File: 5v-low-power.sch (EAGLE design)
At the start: 34 parts, among them J1 Bypass, J2 En, J3 12v, J4 5V Out, J5 LED EN, J6 POWERPOLE_POWER10AWG, J7 POWERPOLE_POWER10AWG, Q1 SI4532ADY, U1 LT1934ES6TRMPBF

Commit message: changed to correct powerpole version added current rating onto docu layer
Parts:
- J6, J7: value POWERPOLE_POWER10AWG -> POWERPOLE_POWER25A; device powerpoles:POWERPOLE_POWER10AWG -> powerpoles:POWERPOLE_POWER25A
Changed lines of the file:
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@@
 <part name="GND" library="testpad" deviceset="TP" device="B1,27" value="5V B"/>
 <part name="J3" library="farnell-parts" deviceset="2-PIN-MOLEX" device="" value="12v"/>
-<part name="J6" library="powerpoles" deviceset="POWERPOLE_POWER" device="10AWG"/>
-<part name="J7" library="powerpoles" deviceset="POWERPOLE_POWER" device="10AWG"/>
+<part name="J6" library="powerpoles" deviceset="POWERPOLE_POWER" device="25A" value="POWERPOLE_POWER25A"/>
+<part name="J7" library="powerpoles" deviceset="POWERPOLE_POWER" device="25A" value="POWERPOLE_POWER25A"/>
 </parts>
 <sheets>

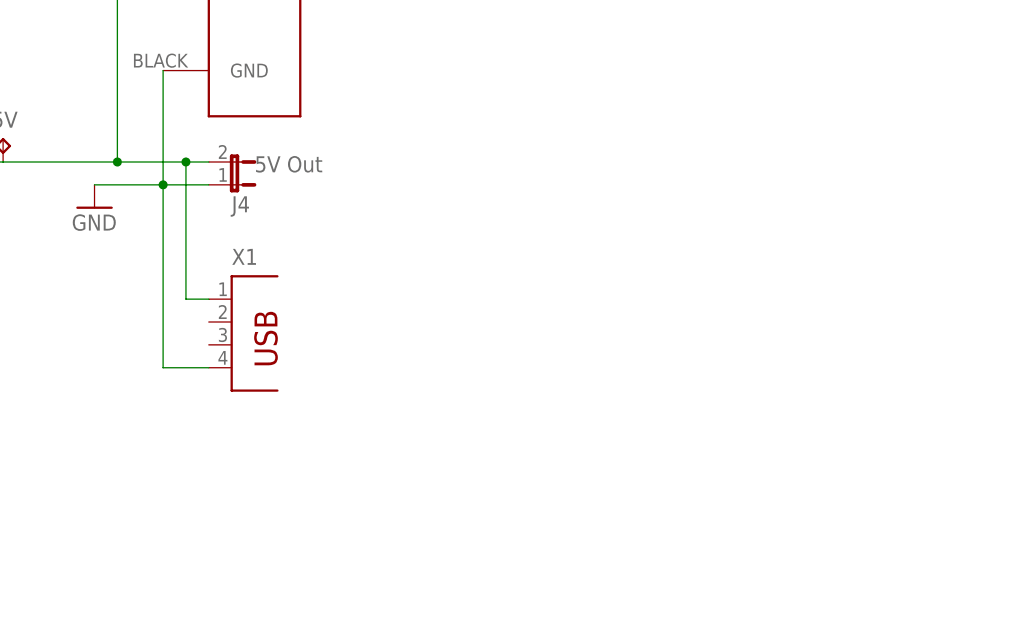
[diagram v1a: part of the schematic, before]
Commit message: Added additional USB footprints and rotated some powerpoles
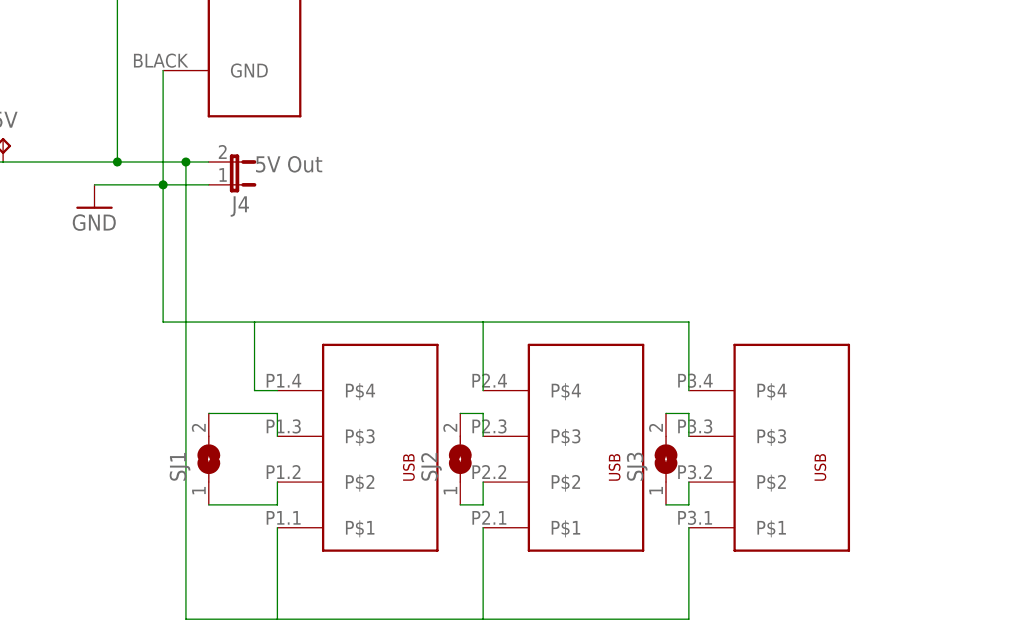
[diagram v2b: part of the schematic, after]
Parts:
- removed X1: (no value), con-berg:PN87520
- added SJ1, SJ2, SJ3: (no value), jumper:SJ
- added U$1: USB_DUAL_VERT+HORIZTRIPPLE, power:USB_DUAL_VERT+HORIZTRIPPLE
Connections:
- new net N$2: SJ1.2, U$1G$1.P$3
- new net N$4: SJ1.1, U$1G$1.P$2
- new net N$5: SJ2.1, U$1G$2.P$2
- new net N$6: SJ2.2, U$1G$2.P$3
- new net N$7: SJ3.2, U$1G$3.P$3
- new net N$8: SJ3.1, U$1G$3.P$2
- net 5V: now also U$1G$1.P$1, U$1G$2.P$1, U$1G$3.P$1; no longer X1.1
- net GND: now also U$1G$1.P$4, U$1G$2.P$4, U$1G$3.P$4; no longer X1.4
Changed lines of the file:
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@@
 <?xml version="1.0" encoding="utf-8"?>
 <!DOCTYPE eagle SYSTEM "eagle.dtd">
-<eagle version="6.5.0">
+<eagle version="6.4">
 <drawing>
 <settings>
@@
 <part name="P+4" library="supply1" deviceset="VCC" device=""/>
 <part name="D4" library="diode" deviceset="DIODE-" device="SMB"/>
-<part name="X1" library="con-berg" deviceset="PN87520" device=""/>
 <part name="GND" library="testpad" deviceset="TP" device="B1,27" value="5V B"/>
 <part name="J3" library="farnell-parts" deviceset="2-PIN-MOLEX" device="" value="12v"/>
 <part name="J6" library="powerpoles" deviceset="POWERPOLE_POWER" device="25A" value="POWERPOLE_POWER25A"/>
 <part name="J7" library="powerpoles" deviceset="POWERPOLE_POWER" device="25A" value="POWERPOLE_POWER25A"/>
+<part name="U$1" library="power" deviceset="USB_DUAL_VERT+HORIZ" device="TRIPPLE"/>
+<part name="SJ1" library="jumper" deviceset="SJ" device=""/>
+<part name="SJ2" library="jumper" deviceset="SJ" device=""/>
+<part name="SJ3" library="jumper" deviceset="SJ" device=""/>
 </parts>
 <sheets>
@@
 <instance part="P+4" gate="VCC" x="81.28" y="226.06"/>
 <instance part="D4" gate="G$1" x="66.04" y="220.98"/>
-<instance part="X1" gate="G$1" x="233.68" y="132.08"/>
 <instance part="GND" gate="G$1" x="109.22" y="180.34"/>
 <instance part="J3" gate="G$1" x="55.88" y="218.44" smashed="yes" rot="R90">
@@
 <instance part="J6" gate="G$1" x="236.22" y="167.64"/>
 <instance part="J7" gate="G$1" x="48.26" y="236.22" rot="MR0"/>
+<instance part="U$1" gate="G$1" x="243.84" y="119.38"/>
+<instance part="U$1" gate="G$2" x="266.7" y="119.38"/>
+<instance part="U$1" gate="G$3" x="289.56" y="119.38"/>
+<instance part="SJ1" gate="1" x="231.14" y="119.38" rot="R90"/>
+<instance part="SJ2" gate="1" x="259.08" y="119.38" rot="R90"/>
+<instance part="SJ3" gate="1" x="281.94" y="119.38" rot="R90"/>
 </instances>
 <busses>
@@
 <pinref part="GND1" gate="1" pin="GND"/>
 <wire x1="231.14" y1="149.86" x2="226.06" y2="149.86" width="0.1524" layer="91"/>
-<pinref part="X1" gate="G$1" pin="4"/>
 <wire x1="226.06" y1="149.86" x2="218.44" y2="149.86" width="0.1524" layer="91"/>
-<wire x1="231.14" y1="129.54" x2="226.06" y2="129.54" width="0.1524" layer="91"/>
-<wire x1="226.06" y1="129.54" x2="226.06" y2="149.86" width="0.1524" layer="91"/>
 <junction x="226.06" y="149.86"/>
 <pinref part="J6" gate="G$1" pin="GND"/>
 <wire x1="226.06" y1="162.56" x2="226.06" y2="149.86" width="0.1524" layer="91"/>
+<wire x1="226.06" y1="149.86" x2="226.06" y2="134.62" width="0.1524" layer="91"/>
+<wire x1="226.06" y1="134.62" x2="236.22" y2="134.62" width="0.1524" layer="91"/>
+<pinref part="U$1" gate="G$1" pin="P$4"/>
+<wire x1="236.22" y1="134.62" x2="236.22" y2="127" width="0.1524" layer="91"/>
+<wire x1="236.22" y1="127" x2="238.76" y2="127" width="0.1524" layer="91"/>
+<pinref part="U$1" gate="G$2" pin="P$4"/>
+<wire x1="236.22" y1="134.62" x2="261.62" y2="134.62" width="0.1524" layer="91"/>
+<wire x1="261.62" y1="134.62" x2="261.62" y2="127" width="0.1524" layer="91"/>
+<pinref part="U$1" gate="G$3" pin="P$4"/>
+<wire x1="261.62" y1="134.62" x2="284.48" y2="134.62" width="0.1524" layer="91"/>
+<wire x1="284.48" y1="134.62" x2="284.48" y2="127" width="0.1524" layer="91"/>
 </segment>
 <segment>
@@
 <pinref part="5V" gate="G$1" pin="TP"/>
 <pinref part="J4" gate="G$1" pin="2"/>
-<pinref part="X1" gate="G$1" pin="1"/>
-<wire x1="231.14" y1="137.16" x2="228.6" y2="137.16" width="0.1524" layer="91"/>
-<wire x1="228.6" y1="137.16" x2="228.6" y2="152.4" width="0.1524" layer="91"/>
 <junction x="228.6" y="152.4"/>
 <pinref part="J6" gate="G$1" pin="V+"/>
@@
 <junction x="220.98" y="152.4"/>
 <wire x1="198.12" y1="152.4" x2="208.28" y2="152.4" width="0.1524" layer="91"/>
+<wire x1="228.6" y1="152.4" x2="228.6" y2="101.6" width="0.1524" layer="91"/>
+<pinref part="U$1" gate="G$1" pin="P$1"/>
+<wire x1="228.6" y1="101.6" x2="238.76" y2="101.6" width="0.1524" layer="91"/>
+<wire x1="238.76" y1="101.6" x2="238.76" y2="111.76" width="0.1524" layer="91"/>
+<pinref part="U$1" gate="G$2" pin="P$1"/>
+<wire x1="238.76" y1="101.6" x2="261.62" y2="101.6" width="0.1524" layer="91"/>
+<wire x1="261.62" y1="101.6" x2="261.62" y2="111.76" width="0.1524" layer="91"/>
+<pinref part="U$1" gate="G$3" pin="P$1"/>
+<wire x1="261.62" y1="101.6" x2="284.48" y2="101.6" width="0.1524" layer="91"/>
+<wire x1="284.48" y1="101.6" x2="284.48" y2="111.76" width="0.1524" layer="91"/>
 </segment>
 </net>
@@
 </segment>
 </net>
+<net name="N$2" class="0">
+<segment>
+<pinref part="SJ1" gate="1" pin="2"/>
+<pinref part="U$1" gate="G$1" pin="P$3"/>
+<wire x1="231.14" y1="124.46" x2="238.76" y2="124.46" width="0.1524" layer="91"/>
+<wire x1="238.76" y1="124.46" x2="238.76" y2="121.92" width="0.1524" layer="91"/>
+</segment>
+</net>
+<net name="N$4" class="0">
+<segment>
+<pinref part="U$1" gate="G$1" pin="P$2"/>
+<wire x1="238.76" y1="116.84" x2="238.76" y2="114.3" width="0.1524" layer="91"/>
+<pinref part="SJ1" gate="1" pin="1"/>
+<wire x1="238.76" y1="114.3" x2="231.14" y2="114.3" width="0.1524" layer="91"/>
+</segment>
+</net>
+<net name="N$5" class="0">
+<segment>
+<pinref part="SJ2" gate="1" pin="1"/>
+<pinref part="U$1" gate="G$2" pin="P$2"/>
+<wire x1="259.08" y1="114.3" x2="261.62" y2="114.3" width="0.1524" layer="91"/>
+<wire x1="261.62" y1="114.3" x2="261.62" y2="116.84" width="0.1524" layer="91"/>
+</segment>
+</net>
+<net name="N$6" class="0">
+<segment>
+<pinref part="SJ2" gate="1" pin="2"/>
+<pinref part="U$1" gate="G$2" pin="P$3"/>
+<wire x1="259.08" y1="124.46" x2="261.62" y2="124.46" width="0.1524" layer="91"/>
+<wire x1="261.62" y1="124.46" x2="261.62" y2="121.92" width="0.1524" layer="91"/>
+</segment>
+</net>
+<net name="N$7" class="0">
+<segment>
+<pinref part="SJ3" gate="1" pin="2"/>
+<pinref part="U$1" gate="G$3" pin="P$3"/>
+<wire x1="281.94" y1="124.46" x2="284.48" y2="124.46" width="0.1524" layer="91"/>
+<wire x1="284.48" y1="124.46" x2="284.48" y2="121.92" width="0.1524" layer="91"/>
+</segment>
+</net>
+<net name="N$8" class="0">
+<segment>
+<pinref part="SJ3" gate="1" pin="1"/>
+<pinref part="U$1" gate="G$3" pin="P$2"/>
+<wire x1="281.94" y1="114.3" x2="284.48" y2="114.3" width="0.1524" layer="91"/>
+<wire x1="284.48" y1="114.3" x2="284.48" y2="116.84" width="0.1524" layer="91"/>
+</segment>
+</net>

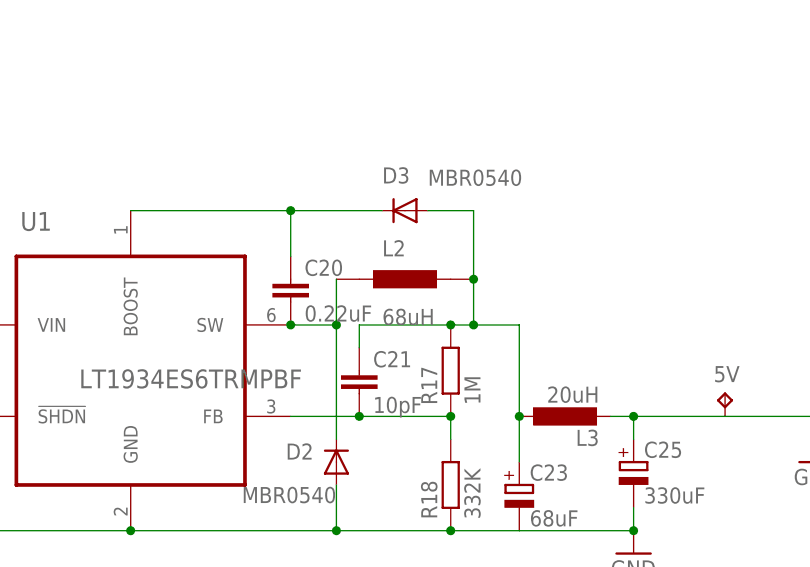
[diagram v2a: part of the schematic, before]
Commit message: now uses DR127 footprint for big inductor
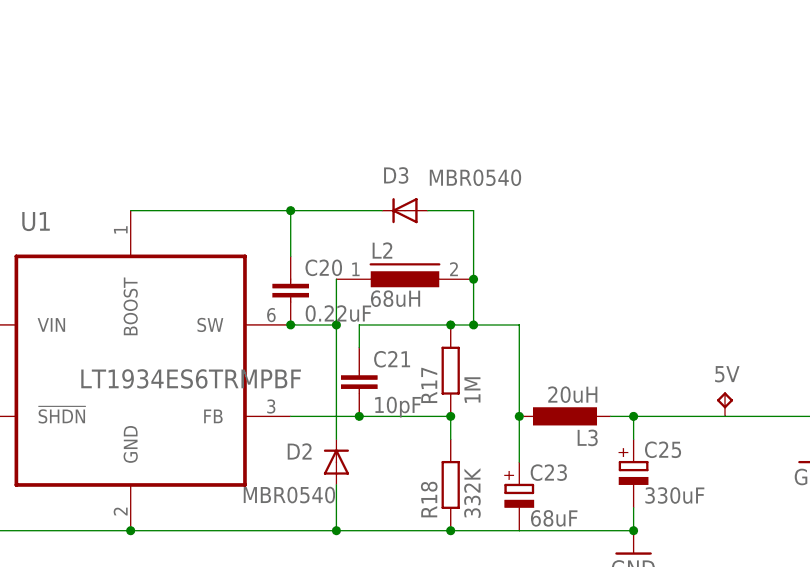
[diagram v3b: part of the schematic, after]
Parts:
- L2: device farnell-parts:SRU1048 -> inductors:DR127
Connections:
- net N$107: now also L2.2; no longer L2.P$2
- net N$78: now also L2.1; no longer L2.P$1
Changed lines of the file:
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@@
 <?xml version="1.0" encoding="utf-8"?>
 <!DOCTYPE eagle SYSTEM "eagle.dtd">
-<eagle version="6.4">
+<eagle version="6.5.0">
 <drawing>
 <settings>
@@
 <part name="R17" library="resistor" deviceset="R-EU_" device="R0805" value="1M"/>
 <part name="C21" library="resistor" deviceset="C-EU" device="C0805" value="10pF"/>
-<part name="L2" library="farnell-parts" deviceset="SRU1048" device="" value="68uH"/>
+<part name="L2" library="inductors" deviceset="DR127" device="" value="68uH"/>
 <part name="C23" library="rcl" deviceset="CPOL-EU" device="E" value="68uF"/>
 <part name="D3" library="diode" deviceset="MBR0520LT" device="" value="MBR0540"/>
@@
 <instance part="R17" gate="G$1" x="177.8" y="157.48" rot="R90"/>
 <instance part="C21" gate="G$1" x="167.64" y="157.48"/>
-<instance part="L2" gate="A" x="172.72" y="167.64"/>
+<instance part="L2" gate="G$1" x="172.72" y="167.64"/>
 <instance part="C23" gate="G$1" x="185.42" y="144.78"/>
 <instance part="D3" gate="G$1" x="172.72" y="175.26" smashed="yes" rot="R180">
@@
 <pinref part="C20" gate="G$1" pin="2"/>
 <pinref part="D2" gate="G$1" pin="C"/>
-<pinref part="L2" gate="A" pin="P$1"/>
+<pinref part="L2" gate="G$1" pin="1"/>
 </segment>
 </net>
@@
 <pinref part="C23" gate="G$1" pin="+"/>
 <pinref part="D3" gate="G$1" pin="A"/>
-<pinref part="L2" gate="A" pin="P$2"/>
+<pinref part="L2" gate="G$1" pin="2"/>
 <pinref part="R17" gate="G$1" pin="2"/>
 <pinref part="C21" gate="G$1" pin="1"/>

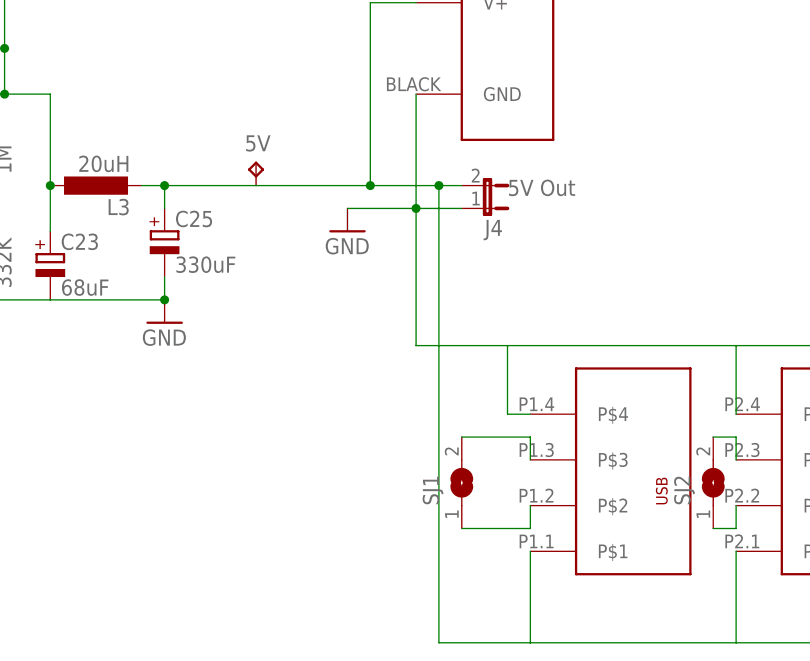
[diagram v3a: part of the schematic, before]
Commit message: Added more smoothing caps
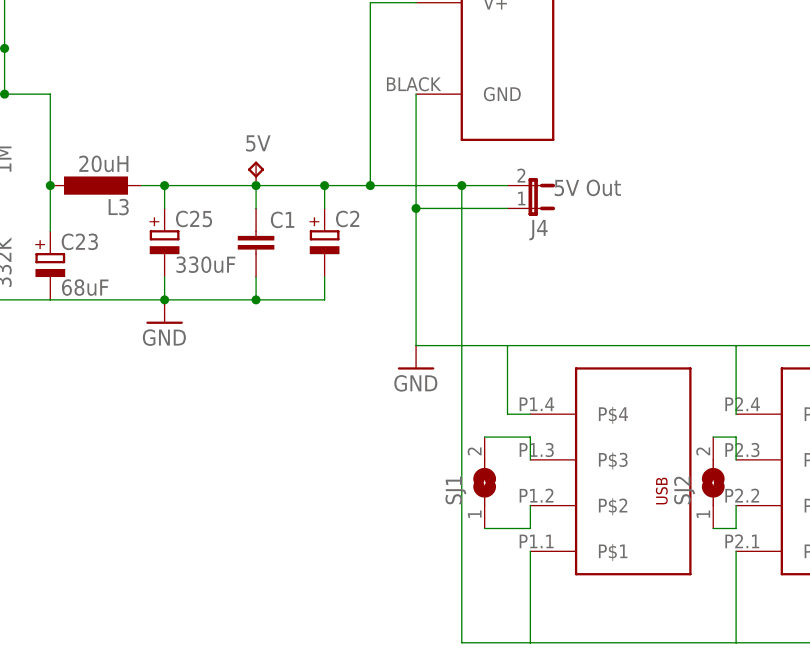
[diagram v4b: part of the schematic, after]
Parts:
- added C1: (no value), resistor:C-EUC0805
- added C2: (no value), resistor:CPOL-EUB/3528-21R
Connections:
- net 5V: now also C1.1, C2.+
- net GND: now also C1.2, C2.-
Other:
- moved on the sheet: J4, SJ1
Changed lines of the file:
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@@
 <part name="SJ2" library="jumper" deviceset="SJ" device=""/>
 <part name="SJ3" library="jumper" deviceset="SJ" device=""/>
+<part name="C1" library="resistor" deviceset="C-EU" device="C0805"/>
+<part name="C2" library="resistor" deviceset="CPOL-EU" device="B/3528-21R"/>
 </parts>
 <sheets>
@@
 <attribute name="VALUE" x="347.98" y="186.055" size="1.778" layer="96" rot="MR180"/>
 </instance>
-<instance part="J4" gate="G$1" x="233.68" y="149.86" smashed="yes" rot="MR90">
-<attribute name="NAME" x="233.68" y="148.59" size="1.778" layer="95" rot="MR180"/>
-<attribute name="VALUE" x="236.22" y="153.035" size="1.778" layer="96" rot="MR180"/>
-</instance>
-<instance part="GND1" gate="1" x="218.44" y="147.32"/>
+<instance part="J4" gate="G$1" x="238.76" y="149.86" smashed="yes" rot="MR90">
+<attribute name="NAME" x="238.76" y="148.59" size="1.778" layer="95" rot="MR180"/>
+<attribute name="VALUE" x="241.3" y="153.035" size="1.778" layer="96" rot="MR180"/>
+</instance>
+<instance part="GND1" gate="1" x="226.06" y="132.08"/>
 <instance part="LED1" gate="G$1" x="330.2" y="195.58"/>
 <instance part="R1" gate="G$1" x="330.2" y="205.74" rot="R90"/>
@@
 <instance part="U$1" gate="G$2" x="266.7" y="119.38"/>
 <instance part="U$1" gate="G$3" x="289.56" y="119.38"/>
-<instance part="SJ1" gate="1" x="231.14" y="119.38" rot="R90"/>
+<instance part="SJ1" gate="1" x="233.68" y="119.38" rot="R90"/>
 <instance part="SJ2" gate="1" x="259.08" y="119.38" rot="R90"/>
 <instance part="SJ3" gate="1" x="281.94" y="119.38" rot="R90"/>
+<instance part="C1" gate="G$1" x="208.28" y="147.32"/>
+<instance part="C2" gate="G$1" x="215.9" y="147.32"/>
 </instances>
 <busses>
@@
 <wire x1="198.12" y1="139.7" x2="198.12" y2="142.24" width="0.1524" layer="91"/>
 <junction x="198.12" y="139.7"/>
+<pinref part="C2" gate="G$1" pin="-"/>
+<wire x1="198.12" y1="139.7" x2="208.28" y2="139.7" width="0.1524" layer="91"/>
+<wire x1="208.28" y1="139.7" x2="215.9" y2="139.7" width="0.1524" layer="91"/>
+<wire x1="215.9" y1="139.7" x2="215.9" y2="142.24" width="0.1524" layer="91"/>
+<pinref part="C1" gate="G$1" pin="2"/>
+<wire x1="208.28" y1="142.24" x2="208.28" y2="139.7" width="0.1524" layer="91"/>
+<junction x="208.28" y="139.7"/>
 </segment>
 <segment>
@@
 <pinref part="J4" gate="G$1" pin="1"/>
 <pinref part="GND1" gate="1" pin="GND"/>
-<wire x1="231.14" y1="149.86" x2="226.06" y2="149.86" width="0.1524" layer="91"/>
-<wire x1="226.06" y1="149.86" x2="218.44" y2="149.86" width="0.1524" layer="91"/>
+<wire x1="236.22" y1="149.86" x2="226.06" y2="149.86" width="0.1524" layer="91"/>
 <junction x="226.06" y="149.86"/>
 <pinref part="J6" gate="G$1" pin="GND"/>
@@
 <pinref part="L3" gate="G$1" pin="2"/>
 <pinref part="C25" gate="G$1" pin="+"/>
-<wire x1="208.28" y1="152.4" x2="220.98" y2="152.4" width="0.1524" layer="91"/>
-<wire x1="220.98" y1="152.4" x2="228.6" y2="152.4" width="0.1524" layer="91"/>
-<wire x1="228.6" y1="152.4" x2="231.14" y2="152.4" width="0.1524" layer="91"/>
+<wire x1="208.28" y1="152.4" x2="215.9" y2="152.4" width="0.1524" layer="91"/>
+<wire x1="215.9" y1="152.4" x2="220.98" y2="152.4" width="0.1524" layer="91"/>
+<wire x1="220.98" y1="152.4" x2="231.14" y2="152.4" width="0.1524" layer="91"/>
+<wire x1="231.14" y1="152.4" x2="236.22" y2="152.4" width="0.1524" layer="91"/>
 <pinref part="5V" gate="G$1" pin="TP"/>
 <pinref part="J4" gate="G$1" pin="2"/>
-<junction x="228.6" y="152.4"/>
+<junction x="231.14" y="152.4"/>
 <pinref part="J6" gate="G$1" pin="V+"/>
 <wire x1="226.06" y1="172.72" x2="220.98" y2="172.72" width="0.1524" layer="91"/>
@@
 <junction x="220.98" y="152.4"/>
 <wire x1="198.12" y1="152.4" x2="208.28" y2="152.4" width="0.1524" layer="91"/>
-<wire x1="228.6" y1="152.4" x2="228.6" y2="101.6" width="0.1524" layer="91"/>
+<wire x1="231.14" y1="152.4" x2="231.14" y2="101.6" width="0.1524" layer="91"/>
 <pinref part="U$1" gate="G$1" pin="P$1"/>
-<wire x1="228.6" y1="101.6" x2="238.76" y2="101.6" width="0.1524" layer="91"/>
+<wire x1="231.14" y1="101.6" x2="238.76" y2="101.6" width="0.1524" layer="91"/>
 <wire x1="238.76" y1="101.6" x2="238.76" y2="111.76" width="0.1524" layer="91"/>
 <pinref part="U$1" gate="G$2" pin="P$1"/>
@@
 <wire x1="261.62" y1="101.6" x2="284.48" y2="101.6" width="0.1524" layer="91"/>
 <wire x1="284.48" y1="101.6" x2="284.48" y2="111.76" width="0.1524" layer="91"/>
+<pinref part="C2" gate="G$1" pin="+"/>
+<wire x1="215.9" y1="152.4" x2="215.9" y2="149.86" width="0.1524" layer="91"/>
+<pinref part="C1" gate="G$1" pin="1"/>
+<wire x1="208.28" y1="149.86" x2="208.28" y2="152.4" width="0.1524" layer="91"/>
+<junction x="208.28" y="152.4"/>
+<junction x="215.9" y="152.4"/>
 </segment>
 </net>
@@
 <pinref part="SJ1" gate="1" pin="2"/>
 <pinref part="U$1" gate="G$1" pin="P$3"/>
-<wire x1="231.14" y1="124.46" x2="238.76" y2="124.46" width="0.1524" layer="91"/>
+<wire x1="233.68" y1="124.46" x2="238.76" y2="124.46" width="0.1524" layer="91"/>
 <wire x1="238.76" y1="124.46" x2="238.76" y2="121.92" width="0.1524" layer="91"/>
 </segment>
@@
 <wire x1="238.76" y1="116.84" x2="238.76" y2="114.3" width="0.1524" layer="91"/>
 <pinref part="SJ1" gate="1" pin="1"/>
-<wire x1="238.76" y1="114.3" x2="231.14" y2="114.3" width="0.1524" layer="91"/>
-</segment>
-</net>
+<wire x1="238.76" y1="114.3" x2="233.68" y2="114.3" width="0.1524" layer="91"/>
+</segment>
+</net>
